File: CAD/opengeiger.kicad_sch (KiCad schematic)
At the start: 90 parts, among them J1 Conn_01x04, J10 Conn_01x04, J3 Conn_01x06, J5 Conn_01x04, J8 USB_C_Receptacle_USB2.0, Q1 STN0214, Q2 PMBT2222A,215, Q3 DMG2302UK-7, Q4 UMH3N, SW1 TL3301NF160QG/TR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

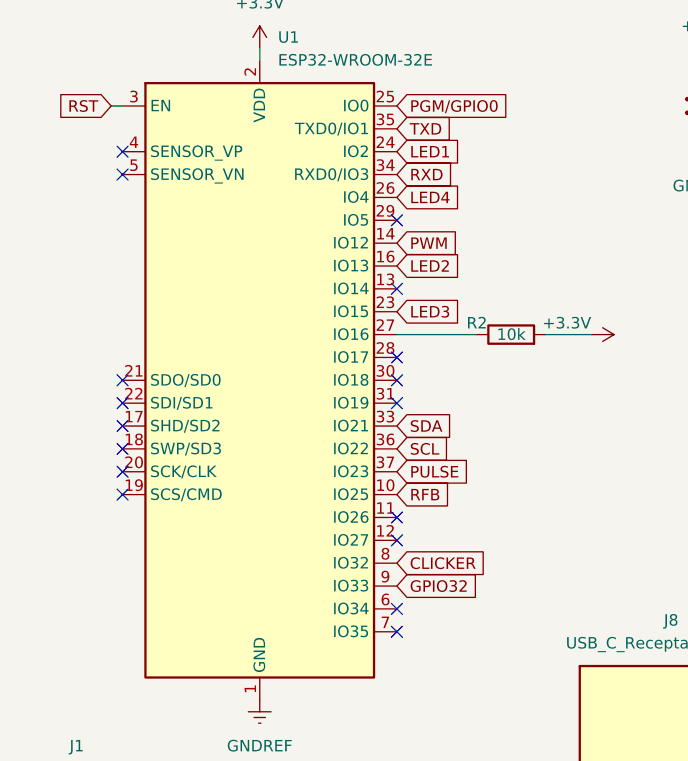
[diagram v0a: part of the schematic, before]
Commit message: Feat: Fixed adc port and captive portal
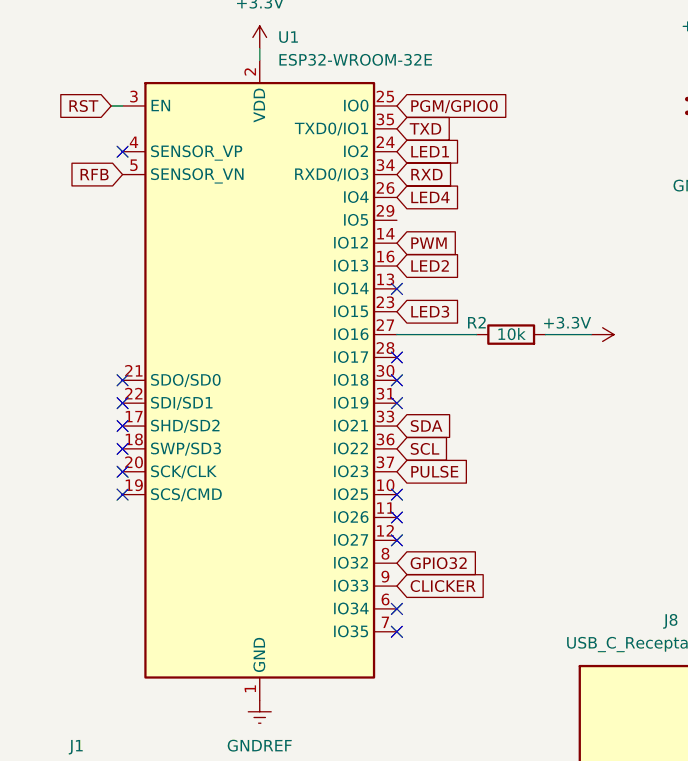
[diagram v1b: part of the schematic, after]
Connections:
- net CLICKER: now also U1.9 (IO33); no longer U1.8 (IO32)
- net GPIO32: now also U1.8 (IO32); no longer U1.9 (IO33)
- net RFB: now also U1.5 (SENSOR_VN); no longer U1.10 (IO25)
- no-connect marks 29 -> 28
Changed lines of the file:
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@@
   )
   (no_connect (at 53.34 81.28))
+  (no_connect (at 53.34 71.12))
   (no_connect (at 53.34 73.66))
-  (no_connect (at 53.34 71.12))
   (no_connect (at 151.13 110.49))
   (no_connect (at 151.13 105.41))
@@
   (no_connect (at 22.86 66.04))
   (no_connect (at 22.86 30.48))
-  (no_connect (at 22.86 33.02))
   (no_connect (at 99.06 118.11))
   (no_connect (at 99.06 120.65))
@@
   (no_connect (at 270.51 31.75))
   (no_connect (at 257.81 22.86))
-  (no_connect (at 53.34 38.1))
+  (no_connect (at 53.34 68.58))
   (no_connect (at 53.34 58.42))
   (no_connect (at 53.34 55.88))
@@
     )
   )
-  (global_label "RFB" (shape input) (at 53.34 68.58 0) (fields_autoplaced)
-    (effects (font (size 1.27 1.27)) (justify left))
-    (property "Intersheet References" "${INTERSHEET_REFS}" (id 0) (at 59.3817 68.6594 0)
-      (effects (font (size 1.27 1.27)) (justify left) hide)
+  (global_label "RFB" (shape input) (at 22.86 33.02 180) (fields_autoplaced)
+    (effects (font (size 1.27 1.27)) (justify right))
+    (property "Intersheet References" "${INTERSHEET_REFS}" (id 0) (at 16.8183 32.9406 0)
+      (effects (font (size 1.27 1.27)) (justify right) hide)
     )
   )
@@
     )
   )
-  (global_label "CLICKER" (shape input) (at 53.34 76.2 0) (fields_autoplaced)
-    (effects (font (size 1.27 1.27)) (justify left))
-    (property "Intersheet References" "${INTERSHEET_REFS}" (id 0) (at 63.615 76.2794 0)
+  (global_label "CLICKER" (shape input) (at 53.34 78.74 0) (fields_autoplaced)
+    (effects (font (size 1.27 1.27)) (justify left))
+    (property "Intersheet References" "${INTERSHEET_REFS}" (id 0) (at 63.615 78.8194 0)
       (effects (font (size 1.27 1.27)) (justify left) hide)
     )
@@
     )
   )
-  (global_label "GPIO32" (shape input) (at 53.34 78.74 0) (fields_autoplaced)
-    (effects (font (size 1.27 1.27)) (justify left))
-    (property "Intersheet References" "${INTERSHEET_REFS}" (id 0) (at 62.6474 78.8194 0)
-      (effects (font (size 1.27 1.27)) (justify left) hide)
-    )
+  (global_label "GPIO32" (shape input) (at 53.34 76.2 0) (fields_autoplaced)
+    (effects (font (size 1.27 1.27)) (justify left))
+    (property "Intersheet References" "${INTERSHEET_REFS}" (id 0) (at 62.6474 76.2794 0)
+      (effects (font (size 1.27 1.27)) (justify left) hide)
+    )
